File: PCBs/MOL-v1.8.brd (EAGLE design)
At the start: 165.1 x 77.1 mm, 61 parts, among them IC1 ULN2803, IC2 ULN2803, J1 SERVO 1, J2 SERVO 2, U1 SN74LVC2G04DBV, U2 JOYSTICKPTH, U3 JOYSTICKPTH

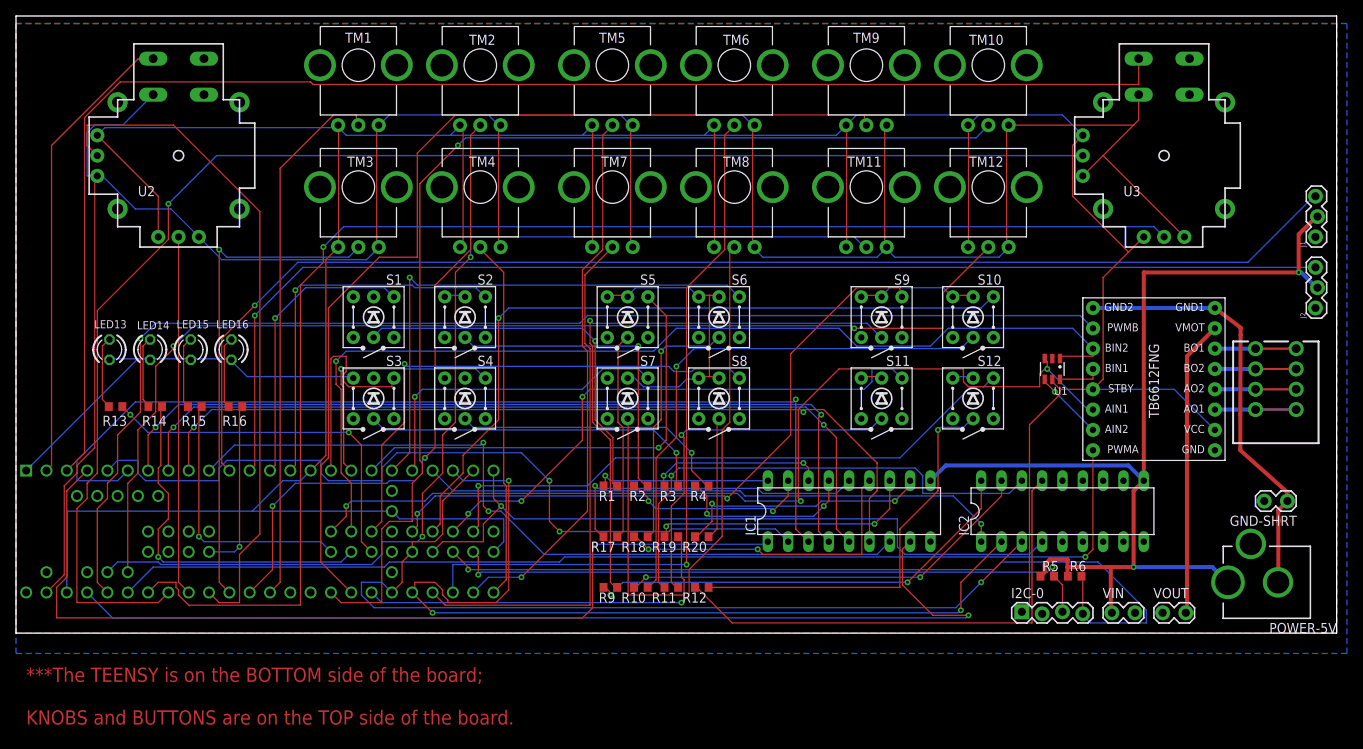
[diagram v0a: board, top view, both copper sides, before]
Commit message: bigger traces
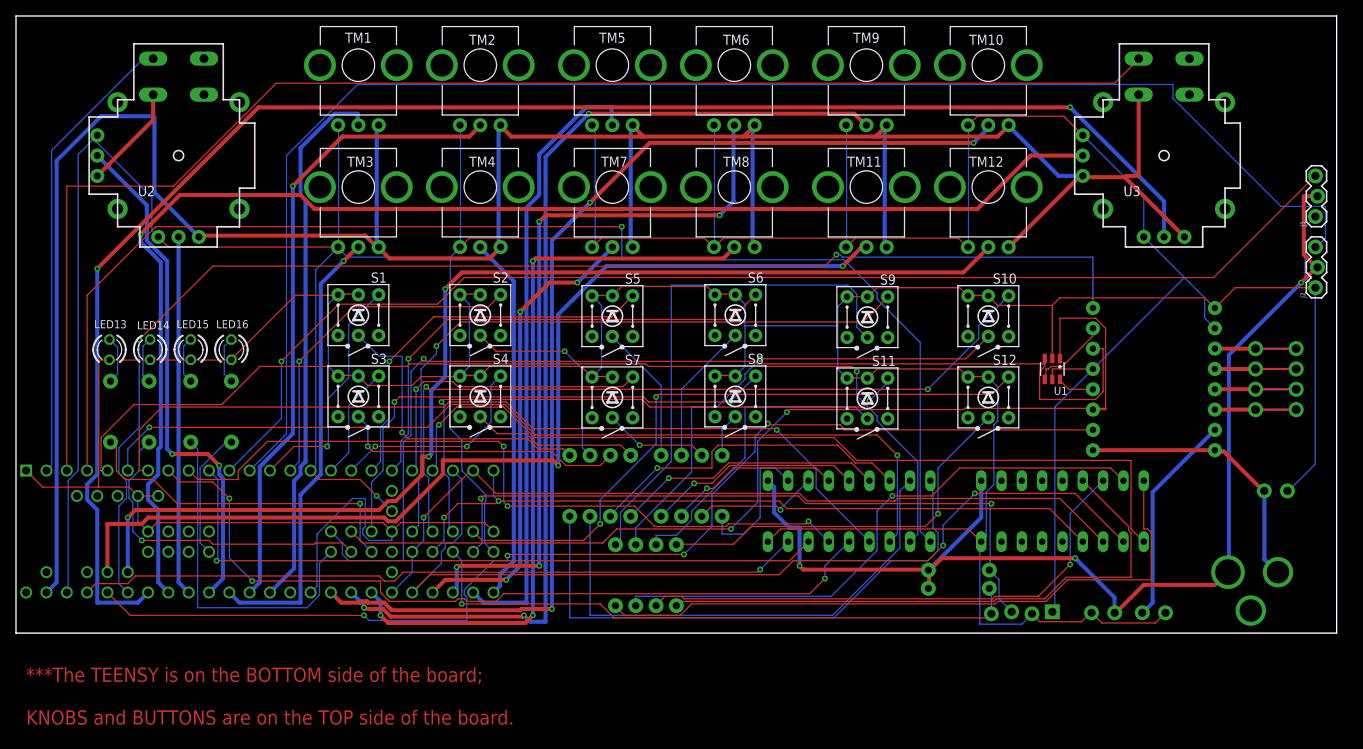
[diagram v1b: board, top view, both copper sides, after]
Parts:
- R1, R10, R11, R12, R13, R14, R15, R16, R17, R18, R19, R2, R20, R3, R4, R5, R6, R9: device CMU-ArtFab:R0603 -> SparkFun-Resistors:AXIAL-0.3EZ
- moved R6 14.6 mm to (117.9, 5.59), flipped to the bottom, turned to 180 degrees
- moved R5 11.1 mm to (117.9, 7.87), flipped to the bottom, turned to 180 degrees
- moved R17 8.98 mm to (80.6, 18.4), flipped to the bottom, turned to 270 degrees
- moved R4 8.89 mm to (76.8, 18.4), flipped to the bottom, turned to 270 degrees
- moved R18 8.13 mm to (83.2, 18.4), flipped to the bottom, turned to 270 degrees
- moved R3 7.62 mm to (74.3, 18.4), flipped to the bottom, turned to 270 degrees
- moved MOTORS1 7.62 mm to (157.5, 35.6), flipped to the bottom, turned to 270 degrees
- moved R19 7.41 mm to (85.7, 18.4), flipped to the bottom, turned to 270 degrees
- moved R20 6.84 mm to (88.3, 18.4), flipped to the bottom, turned to 270 degrees
- moved R2 6.35 mm to (71.8, 18.4), flipped to the bottom, turned to 270 degrees
- moved R1 5.08 mm to (69.2, 18.4), flipped to the bottom, turned to 270 degrees
- moved I2C-0 3.81 mm to (129.5, 2.54), flipped to the bottom
- moved R12 3.52 mm to (82.5, 7.24), flipped to the bottom, turned to 270 degrees
- moved GND-SHRT 2.84 mm to (156.2, 17.8), flipped to the bottom
- moved J1 2.54 mm to (162.6, 52.1)
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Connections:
- net +5V: now also R5.P$1, R6.P$1; no longer R5.1, R6.1
- net I2C_SCL: now also R5.P$2; no longer R5.2
- net I2C_SDA: now also R6.P$2; no longer R6.2
- net LED1: now also R1.P$2; no longer R1.2
- net LED10: now also R10.P$2; no longer R10.2
- net LED11: now also R11.P$2; no longer R11.2
- net LED12: now also R12.P$2; no longer R12.2
- net LED2: now also R2.P$2; no longer R2.2
- net LED3: now also R3.P$2; no longer R3.2
- net LED4: now also R4.P$2; no longer R4.2
- net LED5: now also R17.P$2; no longer R17.2
- net LED6: now also R18.P$2; no longer R18.2
- net LED7: now also R19.P$2; no longer R19.2
- net LED8: now also R20.P$2; no longer R20.2
- net LED9: now also R9.P$2; no longer R9.2
- net N$1: now also R1.P$1; no longer R1.1
- net N$10: now also R4.P$1; no longer R4.1
- net N$15: now also R9.P$1; no longer R9.1
- net N$16: now also R10.P$1; no longer R10.1
- net N$17: now also R11.P$1; no longer R11.1
- net N$18: now also R12.P$1; no longer R12.1
- net N$19: now also R17.P$1; no longer R17.1
- net N$2: now also R13.P$1; no longer R13.1
- net N$20: now also R18.P$1; no longer R18.1
- net N$21: now also R19.P$1; no longer R19.1
- net N$22: now also R20.P$1; no longer R20.1
- net N$3: now also R14.P$1; no longer R14.1
- net N$4: now also R15.P$1; no longer R15.1
- net N$7: now also R16.P$1; no longer R16.1
- net N$8: now also R2.P$1; no longer R2.1
- net N$9: now also R3.P$1; no longer R3.1
- net U1: now also R13.P$2; no longer R13.2
- net U2: now also R14.P$2; no longer R14.2
- net U3: now also R15.P$2; no longer R15.2
- net U4: now also R16.P$2; no longer R16.2
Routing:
- net GND: track 113.6 -> 483.1 mm
- net LED1: track 22.1 -> 71.3 mm, vias 1 -> 0
- net L1: track 117.3 -> 163.9 mm
- net LED2: track 23.5 -> 63.5 mm, vias 2 -> 0
- net L8: track 127.2 -> 90.8 mm
- net L9: track 73.6 -> 107.1 mm
- net S2: track 154.7 -> 187.8 mm, vias 1 -> 0
- net M_PWMA: track 135.3 -> 164.0 mm, vias 1 -> 2
- net I2C_SDA: track 105.6 -> 77.4 mm
- net LED9: track 55.7 -> 82.4 mm, vias 2 -> 0
- net L2: track 101.8 -> 128.4 mm, vias 2 -> 1
- net S_JOYH: track 174.1 -> 200.7 mm, vias 1 -> 2
- net N$21: track 36.7 -> 13.1 mm, vias 0 -> 1
- net M_JOYV: track 84.7 -> 64.4 mm, vias 0 -> 2
- net GND_MOT: track 54.6 -> 34.5 mm
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- removed copper zone on layer 1, net GND
- removed copper zone on layer 16, net GND
